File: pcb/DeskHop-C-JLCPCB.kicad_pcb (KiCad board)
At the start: 2 copper layers, 66.9 x 74.5 mm, 94 parts, among them J201 Debug, J202 Computer, J203 Power, J204 Device, J301 Debug, J302 Computer, J303 Power, J304 Device, Q201 USB Power Switch, Q301 USB Power Switch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

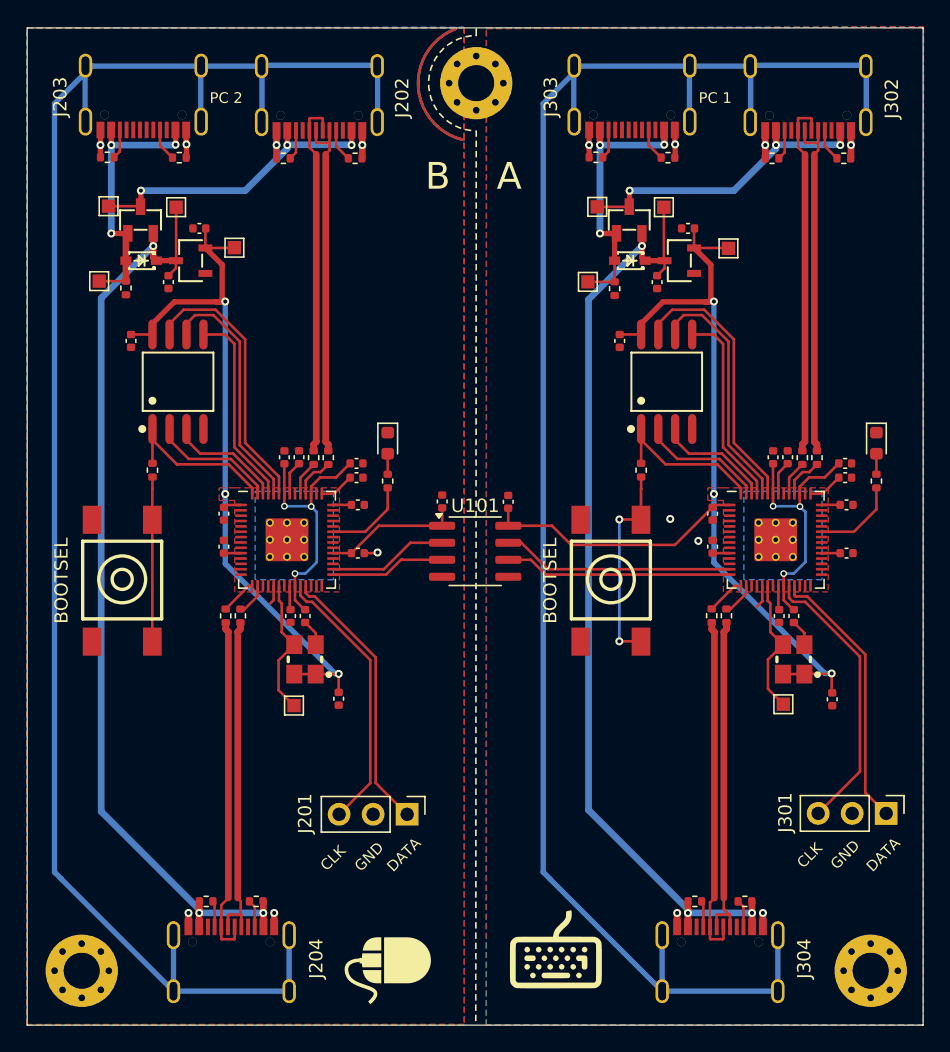
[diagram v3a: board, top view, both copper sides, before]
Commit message: Lots of improvements:
* Modified footprint for USB Type-C connector to use an NPTH for the
  plastic locator pins.

* Connected USB SHIELD to GND as required by the USB spec.

* Simplified trace routing and eliminated most vias.

* Improved VUSB trace routing and sizing.
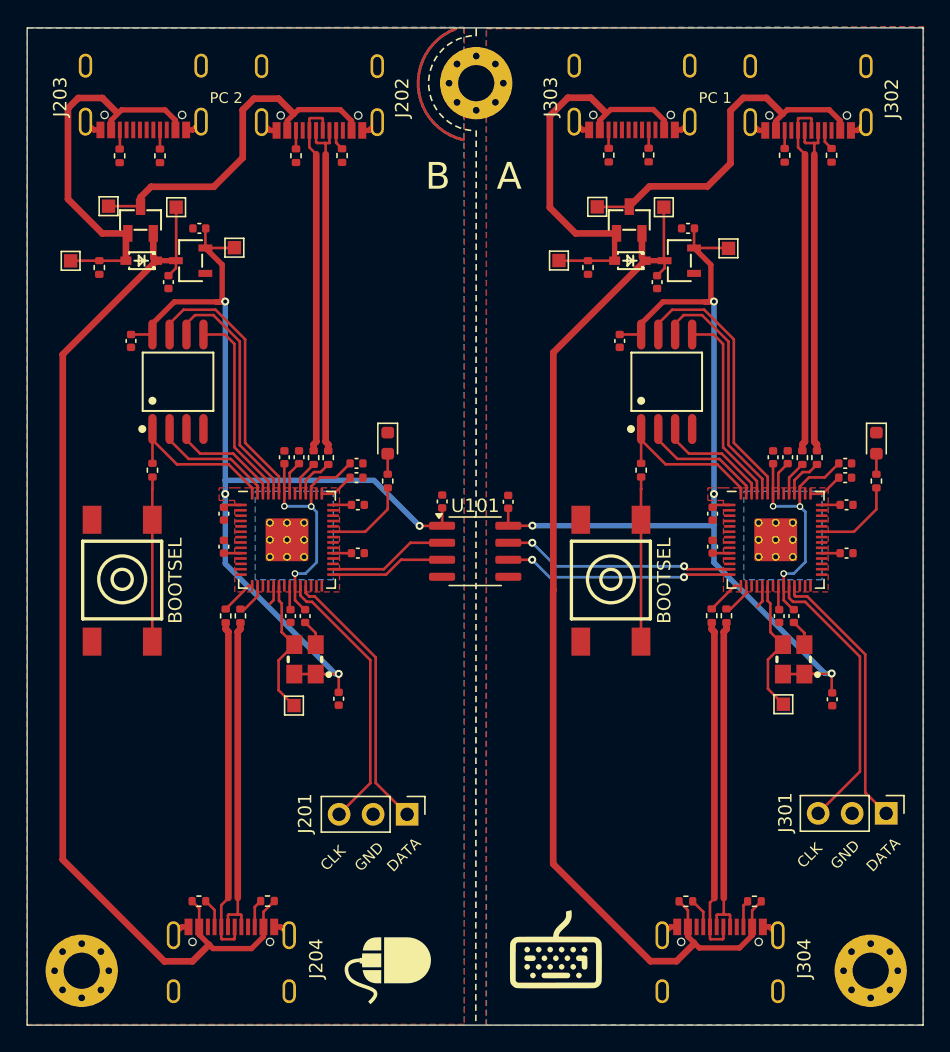
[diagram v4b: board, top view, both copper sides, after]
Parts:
- moved TP301 2.68 mm to (73.5, 58.5)
- moved TP201 2.62 mm to (37.0, 58.5)
- moved R313 2.54 mm to (75.7, 59.0)
- moved R213 2.51 mm to (39.2, 59.0)
- moved R308 1.46 mm to (80.2, 50.6), turned to -90 degrees
- moved R208 1.45 mm to (43.7, 50.6), turned to -90 degrees
- moved R207 1.00 mm to (57.3, 50.6), turned to -90 degrees
- moved R310 0.97 mm to (90.3, 50.6), turned to -90 degrees
- moved R311 0.97 mm to (77.2, 50.6), turned to -90 degrees
- moved R210 0.96 mm to (53.9, 50.6), turned to -90 degrees
- moved R307 0.94 mm to (93.8, 50.6), turned to -90 degrees
- moved R211 0.93 mm to (40.7, 50.6), turned to -90 degrees
- moved R212 0.84 mm to (51.7, 106.3)
- moved R312 0.71 mm to (88.1, 106.3)
- moved R309 0.67 mm to (83.0, 106.3)
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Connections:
- J202 pad 1: /Core Left (B)/SHIELD -> /Core Left (B)/GND
- J202 pad 2: /Core Left (B)/SHIELD -> /Core Left (B)/GND
- J202 pad 3: /Core Left (B)/SHIELD -> /Core Left (B)/GND
- J202 pad 4: /Core Left (B)/SHIELD -> /Core Left (B)/GND
- J203 pad 1: /Core Left (B)/SHIELD -> /Core Left (B)/GND
- J203 pad 2: /Core Left (B)/SHIELD -> /Core Left (B)/GND
- J203 pad 3: /Core Left (B)/SHIELD -> /Core Left (B)/GND
- J203 pad 4: /Core Left (B)/SHIELD -> /Core Left (B)/GND
- J204 pad 1: /Core Left (B)/SHIELD -> /Core Left (B)/GND
- J204 pad 2: /Core Left (B)/SHIELD -> /Core Left (B)/GND
- J204 pad 3: /Core Left (B)/SHIELD -> /Core Left (B)/GND
- J204 pad 4: /Core Left (B)/SHIELD -> /Core Left (B)/GND
- J302 pad 1: /Core Right (A)/SHIELD -> /Core Right (A)/GND
- J302 pad 2: /Core Right (A)/SHIELD -> /Core Right (A)/GND
- J302 pad 3: /Core Right (A)/SHIELD -> /Core Right (A)/GND
- J302 pad 4: /Core Right (A)/SHIELD -> /Core Right (A)/GND
- J303 pad 1: /Core Right (A)/SHIELD -> /Core Right (A)/GND
- J303 pad 2: /Core Right (A)/SHIELD -> /Core Right (A)/GND
- J303 pad 3: /Core Right (A)/SHIELD -> /Core Right (A)/GND
- J303 pad 4: /Core Right (A)/SHIELD -> /Core Right (A)/GND
- J304 pad 1: /Core Right (A)/SHIELD -> /Core Right (A)/GND
- J304 pad 2: /Core Right (A)/SHIELD -> /Core Right (A)/GND
- J304 pad 3: /Core Right (A)/SHIELD -> /Core Right (A)/GND
- J304 pad 4: /Core Right (A)/SHIELD -> /Core Right (A)/GND
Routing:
- net /Core Left (B)/SHIELD: track 129.4 -> 0.00 mm
- net /Core Right (A)/SHIELD: track 128.9 -> 0.00 mm
- net /Core Left (B)/VUSB: track 72.0 -> 82.5 mm, vias 3 -> 0
- net /Core Right (A)/VUSB: track 72.0 -> 82.2 mm, vias 3 -> 0
- net /Core Right (A)/VUSB_PWR: track 20.6 -> 30.7 mm, vias 3 -> 0
- net /Core Left (B)/3V3: track 73.2 -> 83.2 mm, vias 3 -> 4
- net /Core Left (B)/VUSB_PWR: track 20.6 -> 29.8 mm, vias 3 -> 0
- net /Core Left (B)/VUSB_COMP: track 23.2 -> 27.0 mm, vias 3 -> 0
- net /Core Right (A)/VUSB_COMP: track 23.2 -> 26.9 mm, vias 3 -> 0
- net Net-(KEY301-Pad3): track 15.5 -> 12.3 mm, vias 2 -> 0
- net /Core Left (B)/GND: track 14.8 -> 11.7 mm, vias 7 -> 0
- net /Core Right (A)/GND: track 14.0 -> 11.9 mm, vias 8 -> 0
- net /Core Right (A)/3V3: track 83.6 -> 81.9 mm, vias 3 -> 4
- net Net-(J303-CC1): track 2.45 -> 1.36 mm
- net Net-(J203-CC1): track 2.45 -> 1.42 mm
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
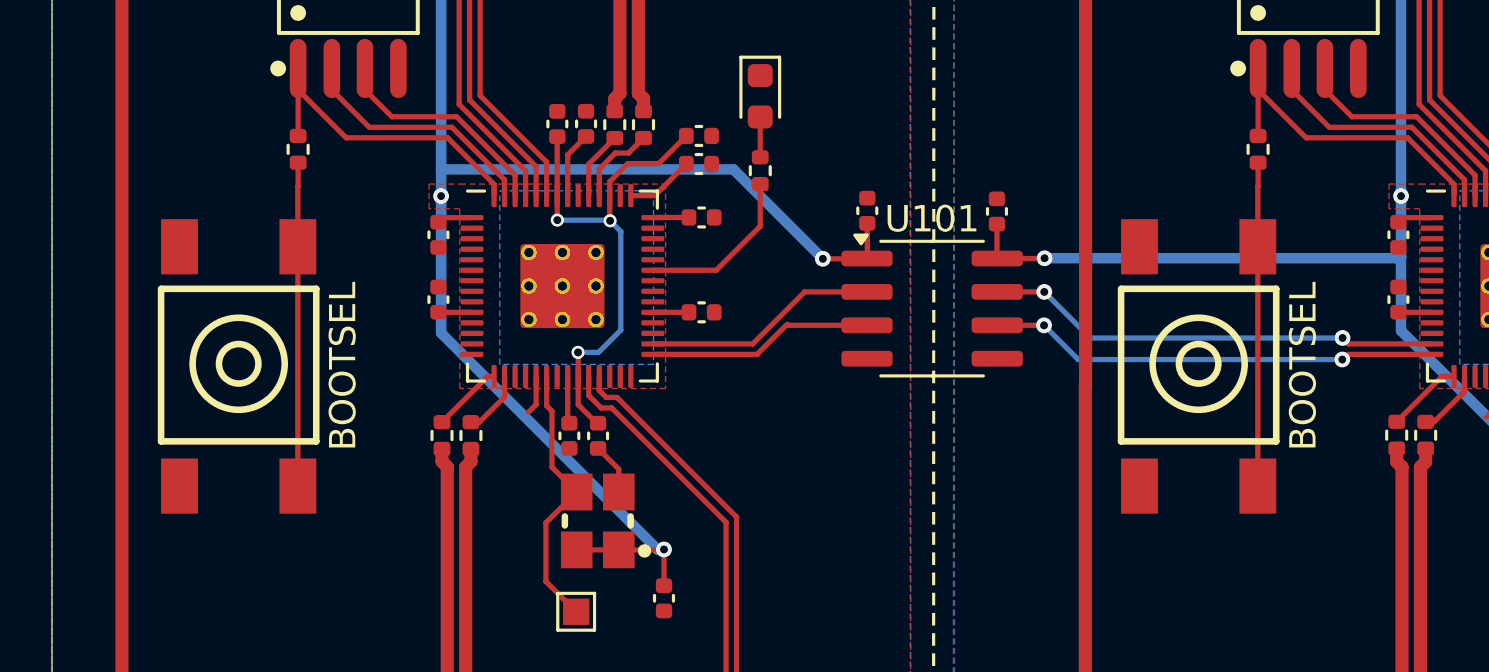
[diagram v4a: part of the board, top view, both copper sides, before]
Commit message: Switch to a smaller pushbutton (similar to the one on the Pico)
Edit imported symbols to use 'LCSC' instead of 'LCSC Part' field name
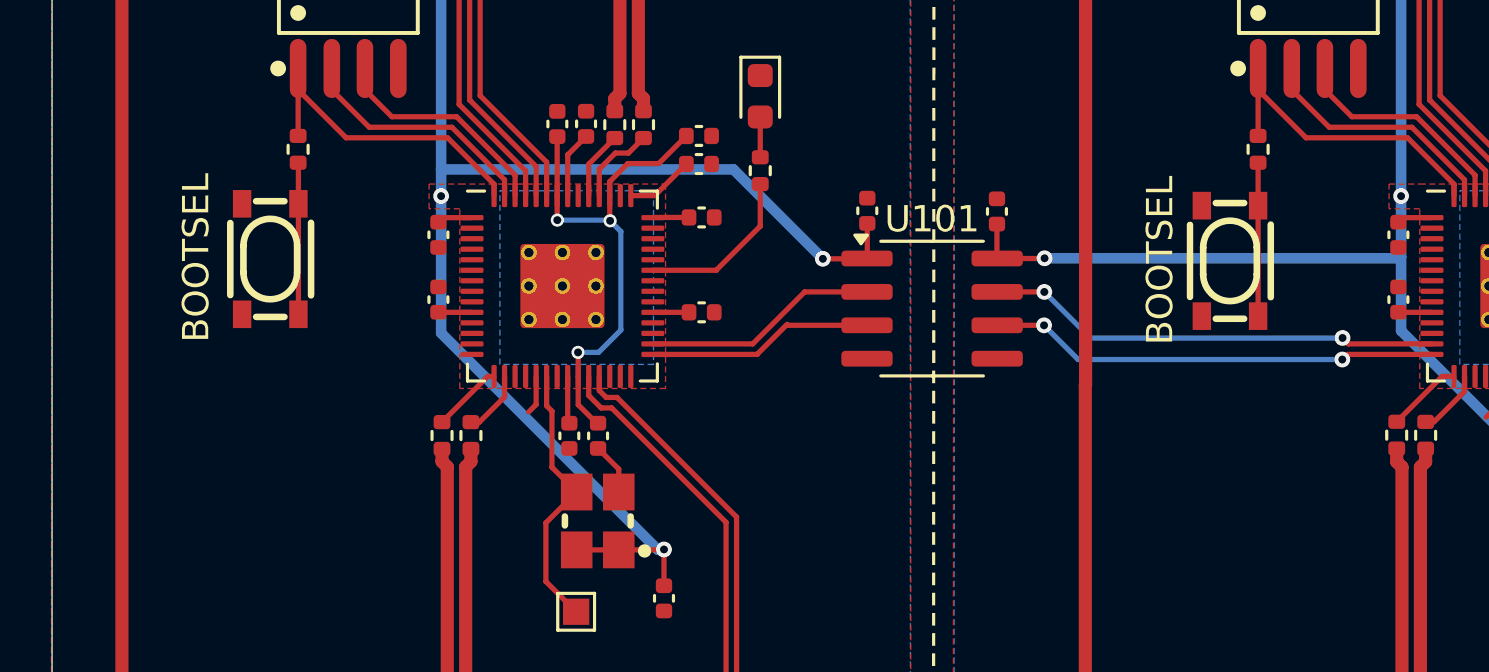
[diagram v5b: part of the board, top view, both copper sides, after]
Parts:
- KEY201, KEY301: footprint LCSC_C86487:KEY-SMD_4P-L6.0-W6.0-P4.50 -> LCSC_C470427:KEY-SMD_4P-L4.2-W3.2-P2.20-LS4.6
- moved KEY201 4.26 mm to (42.1, 78.3), turned to 90 degrees
- moved KEY301 4.19 mm to (78.6, 78.4), turned to 90 degrees
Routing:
- net Net-(KEY201-Pad3): track 12.3 -> 5.77 mm
- net Net-(KEY301-Pad3): track 12.3 -> 5.83 mm
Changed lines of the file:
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@@
       (net 12 "/Core Right (A)/VUSB_PWR") (pinfunction "1") (pintype "passive"))
   )
-  (footprint "LCSC_C86487:KEY-SMD_4P-L6.0-W6.0-P4.50" (layer "F.Cu")
-    (at 77.3686 82.3722 -90)
-    (property "LCSC" "C86487")
-    (property "MPN" "4-1437565-2")
+  (footprint "LCSC_C470427:KEY-SMD_4P-L4.2-W3.2-P2.20-LS4.6" (layer "F.Cu")
+    (at 78.56 78.36 90)
+    (property "LCSC" "C470427")
+    (property "MPN" "SKRPASE010")
     (property "Sheetfile" "core.kicad_sch")
     (property "Sheetname" "Core Right (A)")
     (attr smd)
-    (fp_text reference "KEY301" (at 0 -6.25 90) (layer "F.SilkS") hide
+    (fp_text reference "KEY301" (at 0 -5.07 90) (layer "F.SilkS") hide
         (effects (font (size 1 1) (thickness 0.15)))
     )
-    (fp_text value "BOOTSEL" (at -0.0022 -3.9814 90) (layer "F.SilkS")
+    (fp_text value "BOOTSEL" (at 0.02 -2.66 90) (layer "F.SilkS")
         (effects (font (size 1 1) (thickness 0.15)))
     )
@@
         (effects (font (size 1 1) (thickness 0.15)))
     )
-    (fp_line (start -2.95 -2.95) (end -2.95 2.95)
+    (fp_line (start -2.2 -0.54) (end -2.2 0.54)
       (stroke (width 0.25) (type solid)) (layer "F.SilkS"))
-    (fp_line (start -2.95 2.95) (end 2.85 2.95)
+    (fp_line (start -1.38 1.55) (end 1.38 1.55)
       (stroke (width 0.25) (type solid)) (layer "F.SilkS"))
-    (fp_line (start 2.85 -2.95) (end -2.95 -2.95)
+    (fp_line (start -0.51 -1.02) (end 0.51 -1.02)
       (stroke (width 0.25) (type solid)) (layer "F.SilkS"))
-    (fp_line (start 2.85 2.95) (end 2.85 -2.95)
+    (fp_line (start -0.51 1.02) (end 0.51 1.02)
       (stroke (width 0.25) (type solid)) (layer "F.SilkS"))
-    (fp_circle (center -0.1 0) (end 0.65 0)
-      (stroke (width 0.25) (type solid)) (fill none) (layer "F.SilkS"))
-    (fp_circle (center -0.1 0) (end 1.65 0)
-      (stroke (width 0.25) (type solid)) (fill none) (layer "F.SilkS"))
-    (fp_circle (center 5 3) (end 5.03 3)
+    (fp_line (start 1.37 -1.52) (end -1.37 -1.52)
+      (stroke (width 0.25) (type solid)) (layer "F.SilkS"))
+    (fp_line (start 2.2 -0.54) (end 2.2 0.54)
+      (stroke (width 0.25) (type solid)) (layer "F.SilkS"))
+    (fp_arc (start -0.51 1.02) (mid -1.53 0) (end -0.51 -1.02)
+      (stroke (width 0.25) (type solid)) (layer "F.SilkS"))
+    (fp_arc (start 0.51 -1.02) (mid 1.53 0) (end 0.51 1.02)
+      (stroke (width 0.25) (type solid)) (layer "F.SilkS"))
+    (fp_circle (center -2.3 -1.6) (end -2.27 -1.6)
       (stroke (width 0.06) (type solid)) (fill none) (layer "F.Fab"))
-    (pad "1" smd rect (at 4.55 2.25 270) (size 2.1 1.4) (layers "F.Cu" "F.Paste" "F.Mask")
+    (pad "1" smd rect (at -2.1 -1.07 90) (size 1.05 0.7) (layers "F.Cu" "F.Paste" "F.Mask")
       (net 4 "/Core Right (A)/GND") (pinfunction "1") (pintype "passive"))
-    (pad "2" smd rect (at -4.55 2.25 270) (size 2.1 1.4) (layers "F.Cu" "F.Paste" "F.Mask")
+    (pad "2" smd rect (at 2.1 -1.07 90) (size 1.05 0.7) (layers "F.Cu" "F.Paste" "F.Mask")
       (net 4 "/Core Right (A)/GND") (pinfunction "2") (pintype "passive"))
-    (pad "3" smd rect (at 4.55 -2.25 270) (size 2.1 1.4) (layers "F.Cu" "F.Paste" "F.Mask")
+    (pad "3" smd rect (at -2.1 1.07 90) (size 1.05 0.7) (layers "F.Cu" "F.Paste" "F.Mask")
       (net 44 "Net-(KEY301-Pad3)") (pinfunction "3") (pintype "passive"))
-    (pad "4" smd rect (at -4.55 -2.25 270) (size 2.1 1.4) (layers "F.Cu" "F.Paste" "F.Mask")
+    (pad "4" smd rect (at 2.1 1.07 90) (size 1.05 0.7) (layers "F.Cu" "F.Paste" "F.Mask")
       (net 44 "Net-(KEY301-Pad3)") (pinfunction "4") (pintype "passive"))
-    (model "/home/kpfleming/git-personal/deskhop/pcb/libs/LCSC_C86487.3dshapes/SMD_4P-L6.0-W6.0-H5.0-LS10.0-P4.5.wrl"
+    (model "/home/kpfleming/git-personal/deskhop/pcb/libs/LCSC_C470427.3dshapes/KEY-SMD_4P-L4.2-W3.2-H2.5-LS4.6-P2.2.wrl"
       (offset (xyz 0 -0 -0))
       (scale (xyz 1 1 1))
-      (rotate (xyz 0 0 270))
+      (rotate (xyz 0 0 0))
     )
   )
@@
     )
   )
-  (footprint "LCSC_C86487:KEY-SMD_4P-L6.0-W6.0-P4.50" (layer "F.Cu")
-    (at 40.8686 82.3722 -90)
-    (property "LCSC" "C86487")
-    (property "MPN" "4-1437565-2")
+  (footprint "LCSC_C470427:KEY-SMD_4P-L4.2-W3.2-P2.20-LS4.6" (layer "F.Cu")
+    (at 42.07 78.29 90)
+    (property "LCSC" "C470427")
+    (property "MPN" "SKRPASE010")
     (property "Sheetfile" "core.kicad_sch")
     (property "Sheetname" "Core Left (B)")
     (attr smd)
-    (fp_text reference "KEY201" (at 0 -6.25 90) (layer "F.SilkS") hide
+    (fp_text reference "KEY201" (at 0 -5.07 90) (layer "F.SilkS") hide
         (effects (font (size 1 1) (thickness 0.15)))
     )
-    (fp_text value "BOOTSEL" (at -0.0022 -3.9714 90) (layer "F.SilkS")
+    (fp_text value "BOOTSEL" (at 0.05 -2.82 90) (layer "F.SilkS")
         (effects (font (size 1 1) (thickness 0.15)))
     )
@@
         (effects (font (size 1 1) (thickness 0.15)))
     )
-    (fp_line (start -2.95 -2.95) (end -2.95 2.95)
+    (fp_line (start -2.2 -0.54) (end -2.2 0.54)
       (stroke (width 0.25) (type solid)) (layer "F.SilkS"))
-    (fp_line (start -2.95 2.95) (end 2.85 2.95)
+    (fp_line (start -1.38 1.55) (end 1.38 1.55)
       (stroke (width 0.25) (type solid)) (layer "F.SilkS"))
-    (fp_line (start 2.85 -2.95) (end -2.95 -2.95)
+    (fp_line (start -0.51 -1.02) (end 0.51 -1.02)
       (stroke (width 0.25) (type solid)) (layer "F.SilkS"))
-    (fp_line (start 2.85 2.95) (end 2.85 -2.95)
+    (fp_line (start -0.51 1.02) (end 0.51 1.02)
       (stroke (width 0.25) (type solid)) (layer "F.SilkS"))
-    (fp_circle (center -0.1 0) (end 0.65 0)
-      (stroke (width 0.25) (type solid)) (fill none) (layer "F.SilkS"))
-    (fp_circle (center -0.1 0) (end 1.65 0)
-      (stroke (width 0.25) (type solid)) (fill none) (layer "F.SilkS"))
-    (fp_circle (center 5 3) (end 5.03 3)
+    (fp_line (start 1.37 -1.52) (end -1.37 -1.52)
+      (stroke (width 0.25) (type solid)) (layer "F.SilkS"))
+    (fp_line (start 2.2 -0.54) (end 2.2 0.54)
+      (stroke (width 0.25) (type solid)) (layer "F.SilkS"))
+    (fp_arc (start -0.51 1.02) (mid -1.53 0) (end -0.51 -1.02)
+      (stroke (width 0.25) (type solid)) (layer "F.SilkS"))
+    (fp_arc (start 0.51 -1.02) (mid 1.53 0) (end 0.51 1.02)
+      (stroke (width 0.25) (type solid)) (layer "F.SilkS"))
+    (fp_circle (center -2.3 -1.6) (end -2.27 -1.6)
       (stroke (width 0.06) (type solid)) (fill none) (layer "F.Fab"))
-    (pad "1" smd rect (at 4.55 2.25 270) (size 2.1 1.4) (layers "F.Cu" "F.Paste" "F.Mask")
+    (pad "1" smd rect (at -2.1 -1.07 90) (size 1.05 0.7) (layers "F.Cu" "F.Paste" "F.Mask")
       (net 2 "/Core Left (B)/GND") (pinfunction "1") (pintype "passive"))
-    (pad "2" smd rect (at -4.55 2.25 270) (size 2.1 1.4) (layers "F.Cu" "F.Paste" "F.Mask")
+    (pad "2" smd rect (at 2.1 -1.07 90) (size 1.05 0.7) (layers "F.Cu" "F.Paste" "F.Mask")
       (net 2 "/Core Left (B)/GND") (pinfunction "2") (pintype "passive"))
-    (pad "3" smd rect (at 4.55 -2.25 270) (size 2.1 1.4) (layers "F.Cu" "F.Paste" "F.Mask")
+    (pad "3" smd rect (at -2.1 1.07 90) (size 1.05 0.7) (layers "F.Cu" "F.Paste" "F.Mask")
       (net 43 "Net-(KEY201-Pad3)") (pinfunction "3") (pintype "passive"))
-    (pad "4" smd rect (at -4.55 -2.25 270) (size 2.1 1.4) (layers "F.Cu" "F.Paste" "F.Mask")
+    (pad "4" smd rect (at 2.1 1.07 90) (size 1.05 0.7) (layers "F.Cu" "F.Paste" "F.Mask")
       (net 43 "Net-(KEY201-Pad3)") (pinfunction "4") (pintype "passive"))
-    (model "/home/kpfleming/git-personal/deskhop/pcb/libs/LCSC_C86487.3dshapes/SMD_4P-L6.0-W6.0-H5.0-LS10.0-P4.5.wrl"
+    (model "/home/kpfleming/git-personal/deskhop/pcb/libs/LCSC_C470427.3dshapes/KEY-SMD_4P-L4.2-W3.2-H2.5-LS4.6-P2.2.wrl"
       (offset (xyz 0 -0 -0))
       (scale (xyz 1 1 1))
-      (rotate (xyz 0 0 270))
+      (rotate (xyz 0 0 0))
     )
   )
@@
   (segment (start 84.27 107.11) (end 84.27 108.23) (width 0.2) (layer "F.Cu") (net 42))
   (segment (start 83.48 106.32) (end 84.27 107.11) (width 0.2) (layer "F.Cu") (net 42))
-  (segment (start 43.1186 86.9222) (end 43.1186 77.8222) (width 0.2) (layer "F.Cu") (net 43))
-  (segment (start 43.1186 75.532) (end 43.1186 77.8222) (width 0.2) (layer "F.Cu") (net 43))
-  (segment (start 43.1292 74.6272) (end 43.1292 75.5214) (width 0.2) (layer "F.Cu") (net 43))
-  (segment (start 43.1292 75.5214) (end 43.1186 75.532) (width 0.2) (layer "F.Cu") (net 43))
-  (segment (start 79.6186 75.532) (end 79.6186 77.8222) (width 0.2) (layer "F.Cu") (net 44))
-  (segment (start 79.6292 74.6272) (end 79.6292 75.5214) (width 0.2) (layer "F.Cu") (net 44))
-  (segment (start 79.6292 75.5214) (end 79.6186 75.532) (width 0.2) (layer "F.Cu") (net 44))
-  (segment (start 79.6186 86.9222) (end 79.6186 77.8222) (width 0.2) (layer "F.Cu") (net 44))
+  (segment (start 43.14 80.39) (end 43.14 76.19) (width 0.2) (layer "F.Cu") (net 43))
+  (segment (start 43.14 76.19) (end 43.14 74.638) (width 0.2) (layer "F.Cu") (net 43))
+  (segment (start 43.14 74.638) (end 43.1292 74.6272) (width 0.2) (layer "F.Cu") (net 43))
+  (segment (start 79.6292 80.4592) (end 79.63 80.46) (width 0.2) (layer "F.Cu") (net 44))
+  (segment (start 79.6292 74.6272) (end 79.6292 80.4592) (width 0.2) (layer "F.Cu") (net 44))
   (segment (start 53.676 47.546) (end 54.0306 47.1914) (width 0.4) (layer "F.Cu") (net 45))
   (segment (start 42.2402 54.4322) (end 42.2402 53.7298) (width 0.5) (layer "F.Cu") (net 45))
